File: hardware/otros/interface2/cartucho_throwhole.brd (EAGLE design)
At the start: 41.9 x 34.9 mm, 10 parts, among them IC1 74HC164N, IC2 AM29F010S, IC3 74HC32N

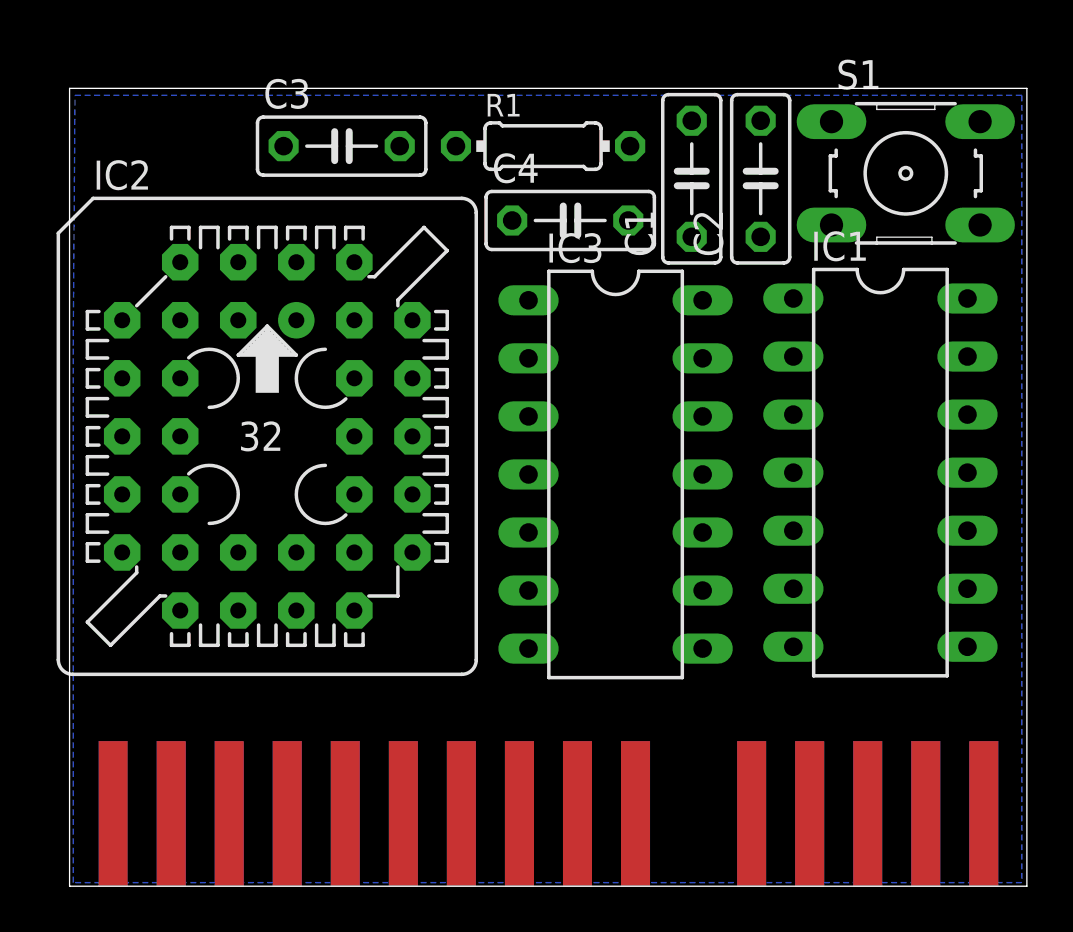
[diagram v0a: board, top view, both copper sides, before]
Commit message: 
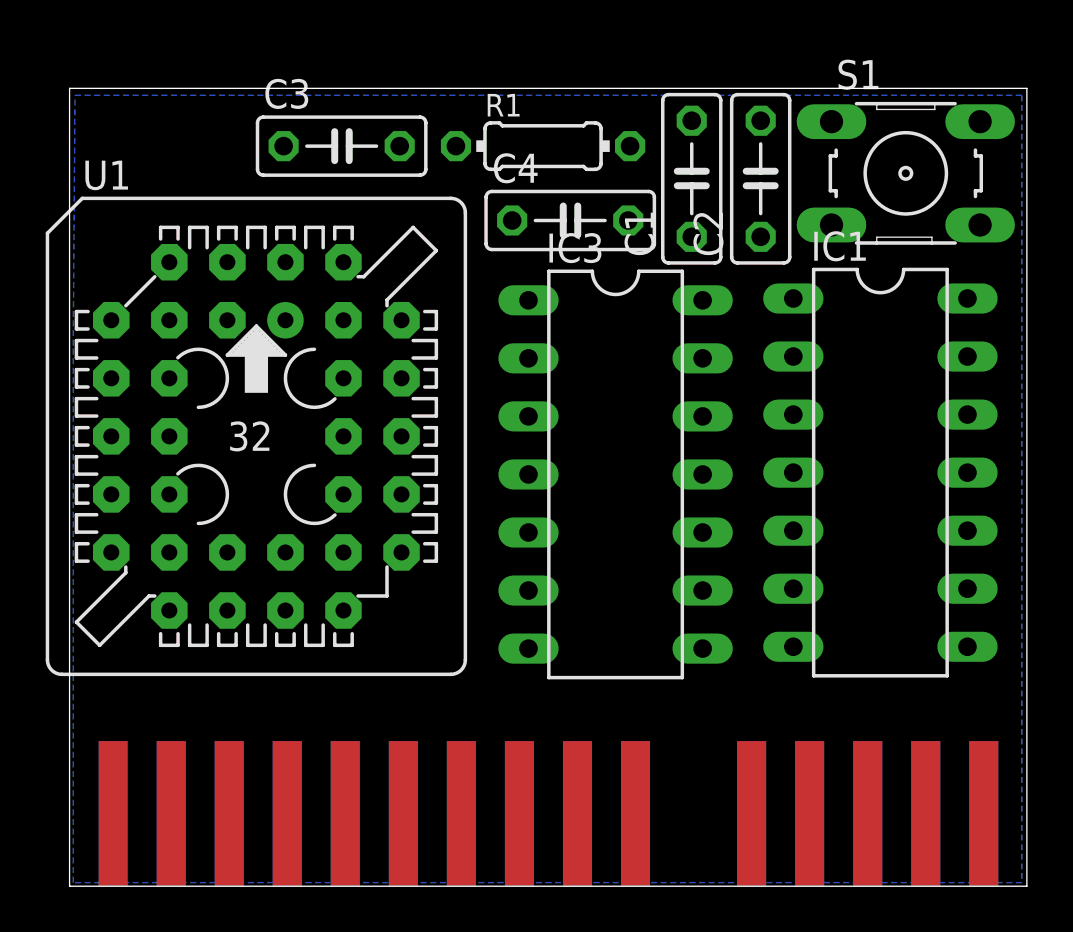
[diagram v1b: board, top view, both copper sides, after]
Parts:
- removed IC2: AM29F010S, am29-memory:PLCC-SR32
- added U1: AM29F040S, am29-memory:PLCC-SR32
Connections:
- net A0: now also U1.12; no longer IC2.12
- net A1: now also U1.11; no longer IC2.11
- net A10: now also U1.23; no longer IC2.23
- net A11: now also U1.25; no longer IC2.25
- net A12: now also U1.4; no longer IC2.4
- net A13: now also U1.28; no longer IC2.28
- net A2: now also U1.10; no longer IC2.10
- net A3: now also U1.9; no longer IC2.9
- net A4: now also U1.8; no longer IC2.8
- net A5: now also U1.7; no longer IC2.7
- net A6: now also U1.6; no longer IC2.6
- net A7: now also U1.5; no longer IC2.5
- net A8: now also U1.27; no longer IC2.27
- net A9: now also U1.26; no longer IC2.26
- net CS: now also U1.22; no longer IC2.22
- net D0: now also U1.13; no longer IC2.13
- net D1: now also U1.14; no longer IC2.14
- net D2: now also U1.15; no longer IC2.15
- net D3: now also U1.17; no longer IC2.17
- net D4: now also U1.18; no longer IC2.18
- net D5: now also U1.19; no longer IC2.19
- net D6: now also U1.20; no longer IC2.20
- net D7: now also U1.21; no longer IC2.21
- net GND: now also U1.16; no longer IC2.16
- net N$2: now also U1.1; no longer IC2.1
- net N$3: now also U1.30; no longer IC2.30
- net N$4: now also U1.2; no longer IC2.2
- net N$5: now also U1.3; no longer IC2.3
- net N$6: now also U1.29; no longer IC2.29
- net RD: now also U1.24; no longer IC2.24
- net VCC: now also U1.32; no longer IC2.32
- net WR: now also U1.31; no longer IC2.31

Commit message: 
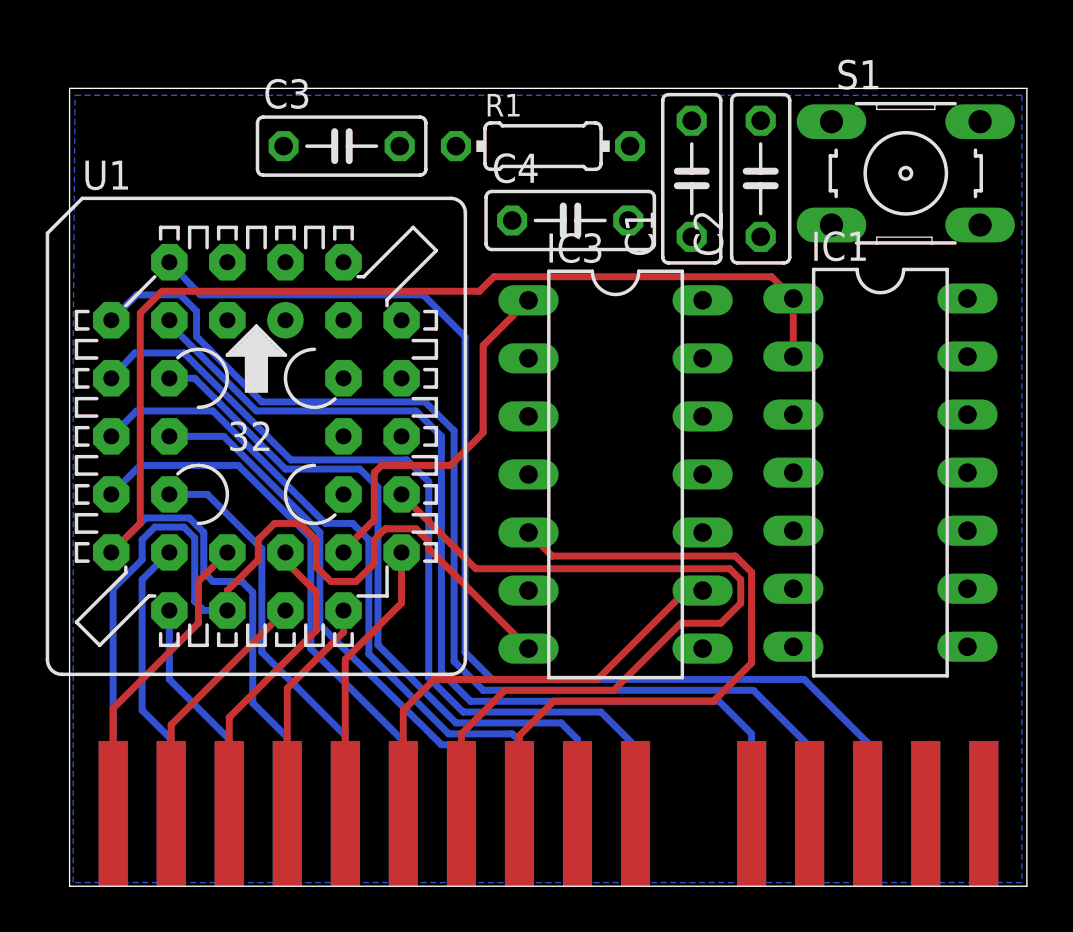
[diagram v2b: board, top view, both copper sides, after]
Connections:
- net A14: now also IC3.9; no longer IC3.4
- net A15: now also IC3.10; no longer IC3.5
- net CS: now also IC3.1; no longer IC3.9
- net MREQ: now also IC3.5; no longer IC3.2
- net N$11: now also IC3.3; no longer IC3.8
- net N$7: now also IC3.4, IC3.8; no longer IC3.1, IC3.6
- net WR: now also IC3.2; no longer IC3.10
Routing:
- net D0: track 0.00 -> 62.7 mm
- net A12: track 0.00 -> 50.5 mm
- net A7: track 0.00 -> 48.7 mm
- net A6: track 0.00 -> 42.6 mm
- net GND: track 0.00 -> 41.1 mm
- net A5: track 0.00 -> 38.5 mm
- net A10: track 0.00 -> 35.5 mm
- net A4: track 0.00 -> 31.7 mm
- net A3: track 0.00 -> 30.4 mm
- net MREQ: track 0.00 -> 29.3 mm
- net A1: track 0.00 -> 24.3 mm
- net A2: track 0.00 -> 23.7 mm
- net A14: track 0.00 -> 19.8 mm
- net A0: track 0.00 -> 18.1 mm
- net CS: track 0.00 -> 16.2 mm
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
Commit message: 
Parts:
- moved C4 4.00 mm to (21.0, 33.0)
- moved R1 2.60 mm to (22.3, 30.3)
- moved IC1 0.08 mm to (35.5, 18.0)
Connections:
- net A14: now also IC3.1; no longer IC3.9
- net A15: now also IC3.2; no longer IC3.10
- net CS: now also IC3.9; no longer IC3.1
- net N$11: now also IC3.8; no longer IC3.3
- net N$7: now also IC3.3; no longer IC3.8
- net WR: now also IC3.10; no longer IC3.2
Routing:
- net GND: track 41.1 -> 89.4 mm
- net A9: track 0.00 -> 46.8 mm
- net A11: track 0.00 -> 44.5 mm
- net A13: track 0.00 -> 43.5 mm
- net A8: track 0.00 -> 41.5 mm
- net A14: track 19.8 -> 39.2 mm
- net MREQ: track 29.3 -> 15.2 mm
- net A10: track 35.5 -> 22.0 mm
- net D0: track 62.7 -> 70.6 mm
- net CS: track 16.2 -> 23.1 mm

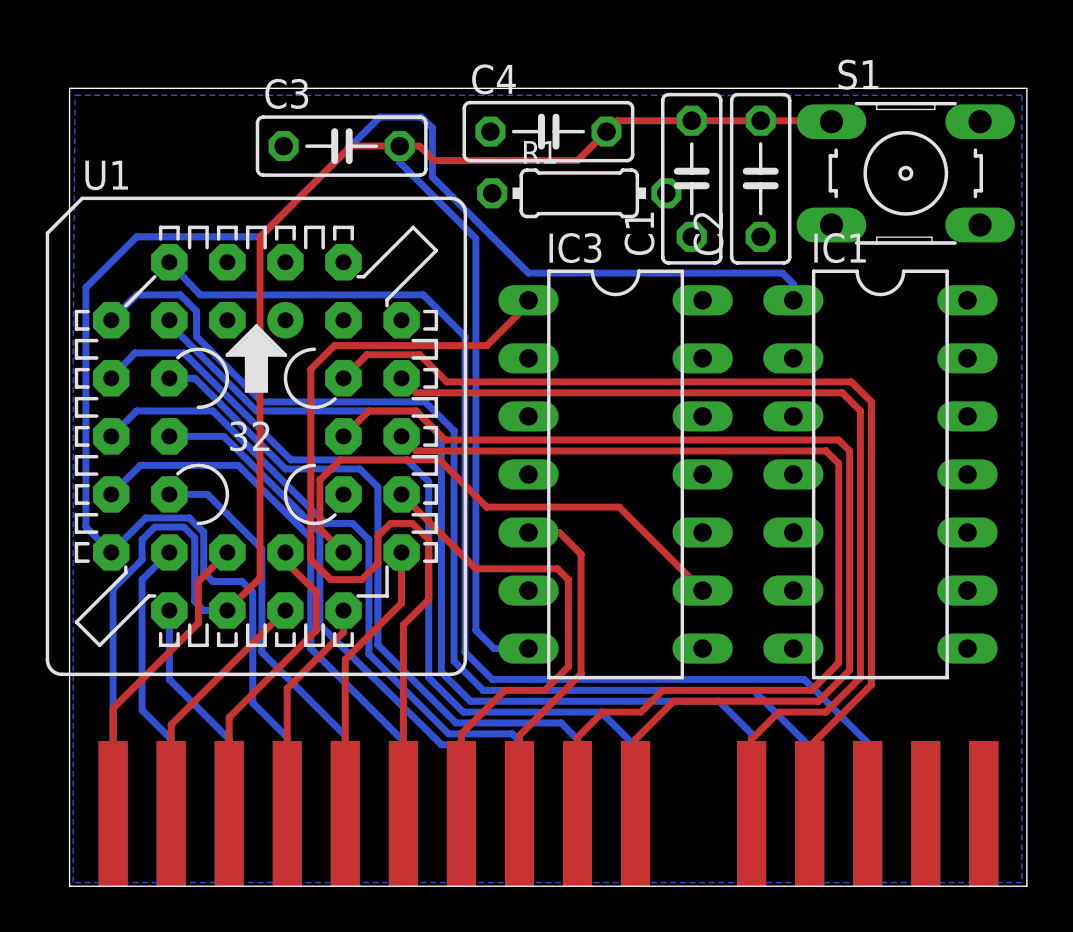
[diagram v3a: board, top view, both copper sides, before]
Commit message: 
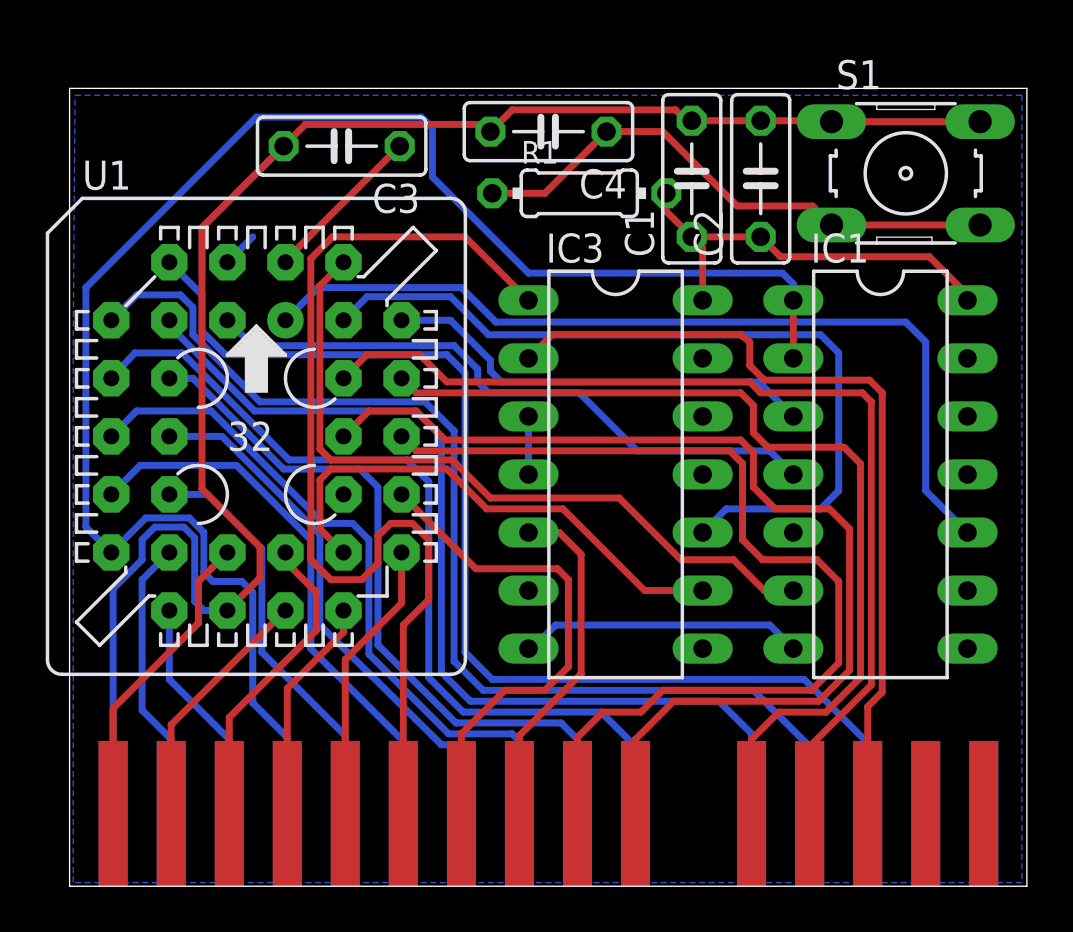
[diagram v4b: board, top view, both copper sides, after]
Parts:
- turned C3 to 180 degrees
- turned C4 to 180 degrees
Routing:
- net N$2: track 0.00 -> 38.7 mm
- net A15: track 0.00 -> 36.2 mm
- net WR: track 0.00 -> 35.9 mm
- net N$3: track 0.00 -> 31.9 mm
- net N$5: track 0.00 -> 27.9 mm
- net VCC: track 0.00 -> 25.8 mm
- net RESET: track 0.00 -> 24.2 mm
- net N$6: track 0.00 -> 19.2 mm
- net GND: track 89.4 -> 95.7 mm
- net A14: track 39.2 -> 44.2 mm
- net D0: track 70.6 -> 73.1 mm
- net N$7: track 0.00 -> 2.54 mm
- net N$4: track 0.00 -> 1.57 mm
- net A9: track 46.8 -> 45.7 mm
- net A11: track 44.5 -> 43.4 mm
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
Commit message: 
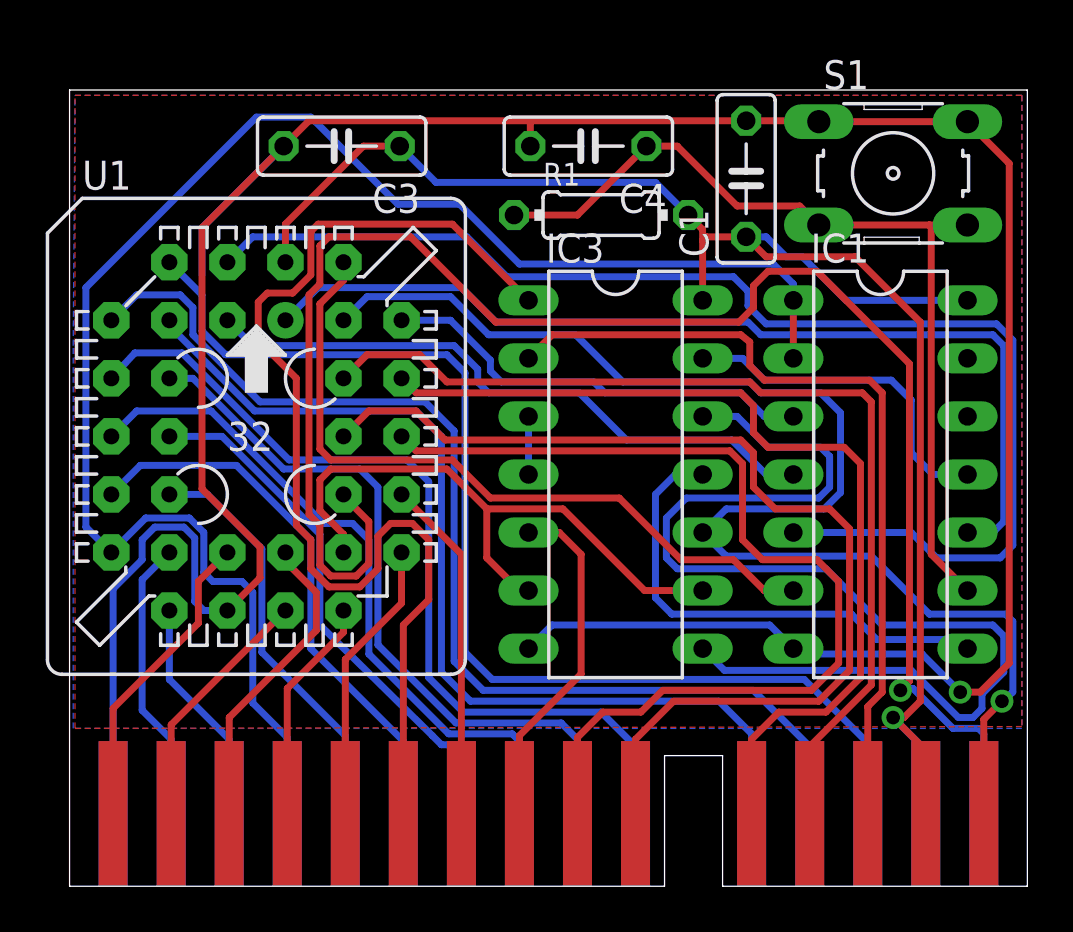
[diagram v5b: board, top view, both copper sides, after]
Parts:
- removed C2: (no value), rcl:C050-025X075
- moved C1 2.38 mm to (29.6, 31.0)
- moved C4 1.86 mm to (22.7, 32.4)
- moved R1 1.35 mm to (23.3, 29.4)
- moved S1 0.56 mm to (36.0, 31.2)
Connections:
- net CS: now also IC3.6
- net GND: no longer C2.2
- net LOCK: now also IC3.13
- net N$11: now also IC3.12
- net VCC: no longer C2.1
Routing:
- net RD: track 0.00 -> 73.6 mm, vias 0 -> 1
- net N$4: track 1.57 -> 56.3 mm
- net N$11: track 0.00 -> 50.5 mm
- net VCC: track 25.8 -> 75.6 mm, vias 0 -> 1
- net GND: track 95.7 -> 131.8 mm, vias 0 -> 1
- net WR: track 35.9 -> 58.7 mm, vias 0 -> 1
- net N$10: track 0.00 -> 21.5 mm
- net RESET: track 24.2 -> 39.9 mm
- net LOCK: track 0.00 -> 15.0 mm
- net A10: track 22.0 -> 15.1 mm
- net CS: track 22.8 -> 27.3 mm
- net A14: track 44.2 -> 48.6 mm
- net N$2: track 38.7 -> 42.6 mm
- net D0: track 73.1 -> 71.9 mm
- added copper zone on layer 1, net VCC
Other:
- board size 41.9 x 34.9 mm -> 41.9 x 34.8 mm
- board text added: "AntonioVillena sep2015"
- board text removed: "AntonioVillena jul2015"

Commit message: 
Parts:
- C1, C3: value (none) -> 100nF
- C4: value (none) -> 4.7uF
- S1: value (none) -> RESET
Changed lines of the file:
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@@
 <elements>
 <element name="U$1" library="SPECTRUM" package="BUS_CARTUCHO_IF2" value="IF2BUS" x="39.37" y="0"/>
-<element name="C1" library="rcl" package="C050-025X075" value="" x="29.606875" y="30.95625" rot="R90"/>
+<element name="C1" library="rcl" package="C050-025X075" value="100nF" x="29.606875" y="30.95625" rot="R90"/>
 <element name="IC1" library="74xx-us" package="DIL14" value="74HC164N" x="35.480625" y="18.018125" rot="R270"/>
-<element name="C3" library="rcl" package="C050-025X075" value="" x="11.90625" y="32.385" rot="R180"/>
-<element name="C4" library="rcl" package="C050-025X075" value="" x="22.70125" y="32.385" rot="R180"/>
+<element name="C3" library="rcl" package="C050-025X075" value="100nF" x="11.90625" y="32.385" rot="R180"/>
+<element name="C4" library="rcl" package="C050-025X075" value="4.7uF" x="22.70125" y="32.385" rot="R180"/>
 <element name="R1" library="rcl" package="0204/7" value="10K" x="23.256875" y="29.36875"/>
-<element name="S1" library="switch-omron" package="B3F-10XX" value="" x="36.03625" y="31.194375">
+<element name="S1" library="switch-omron" package="B3F-10XX" value="RESET" x="36.03625" y="31.194375">
 <attribute name="OC_NEWARK" value="36M3542" x="36.03625" y="31.194375" size="1.778" layer="27" display="off"/>
 <attribute name="MPN" value="B3F-1000" x="36.03625" y="31.194375" size="1.778" layer="27" display="off"/>
@@
 <wire x1="28.654375" y1="9.445625" x2="27.701875" y2="10.398125" width="0.3048" layer="16"/>
 <wire x1="28.654375" y1="9.445625" x2="36.83" y2="9.445625" width="0.3048" layer="16"/>
-<wire x1="36.83" y1="9.445625" x2="38.89375" y2="7.381875" width="0.3048" layer="16"/>
 <wire x1="38.89375" y1="7.381875" x2="39.52875" y2="7.381875" width="0.3048" layer="16"/>
 <wire x1="39.52875" y1="7.381875" x2="39.925625" y2="7.77875" width="0.3048" layer="16"/>
 <wire x1="39.925625" y1="7.77875" x2="39.925625" y2="8.41375" width="0.3048" layer="16"/>
 <wire x1="39.925625" y1="8.41375" x2="40.878125" y2="9.36625" width="0.3048" layer="16"/>
+<wire x1="36.83" y1="9.445625" x2="38.89375" y2="7.381875" width="0.3048" layer="16"/>
 </signal>
 </signals>
